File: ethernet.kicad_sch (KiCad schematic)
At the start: 32 parts

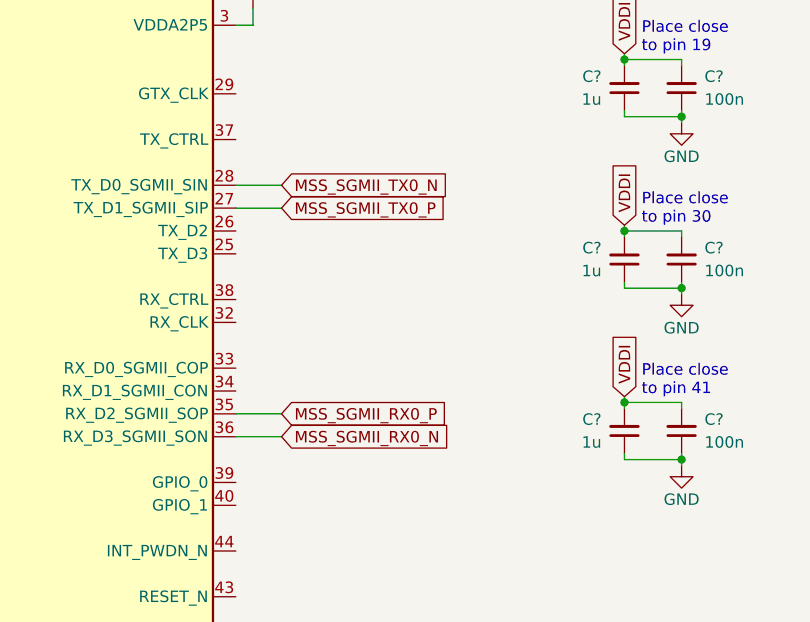
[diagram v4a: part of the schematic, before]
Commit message: [#54016] Add capacitors on SGMII lines
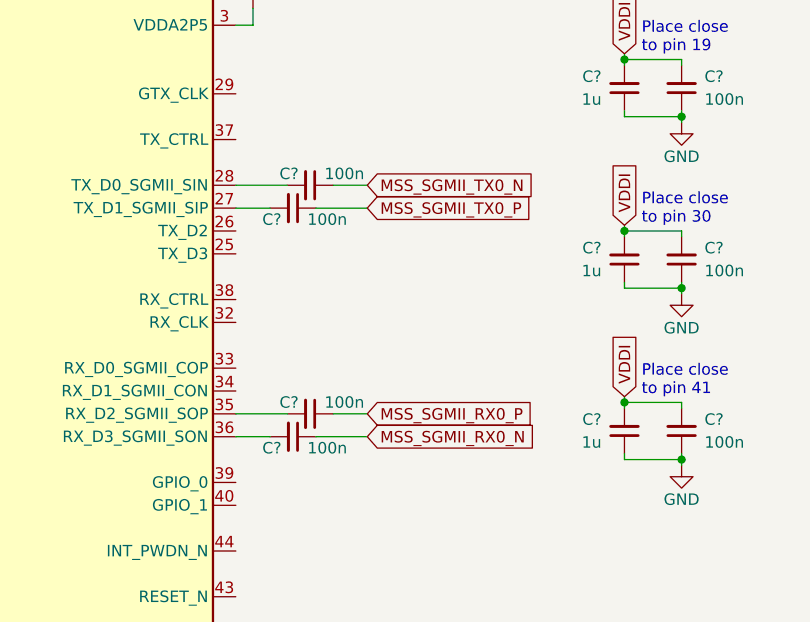
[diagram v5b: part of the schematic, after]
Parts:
- added C? (x4): C_100n_0402, antmicro-footprints:C_0402_1005Metric, symbol antmicroCapacitors0402:C_100n_0402
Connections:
- net MSS_SGMII_RX0_N: now also C?.1; no longer U?.36 (RX_D3_SGMII_SON)
- net MSS_SGMII_RX0_P: now also C?.1; no longer U?.35 (RX_D2_SGMII_SOP)
- net MSS_SGMII_TX0_N: now also C?.1; no longer U?.28 (TX_D0_SGMII_SIN)
- net MSS_SGMII_TX0_P: now also C?.1; no longer U?.27 (TX_D1_SGMII_SIP)
- new net: C?.2, U?.35 (RX_D2_SGMII_SOP)
- new net: C?.2, U?.27 (TX_D1_SGMII_SIP)
- new net: C?.2, U?.28 (TX_D0_SGMII_SIN)
- new net: C?.2, U?.36 (RX_D3_SGMII_SON)

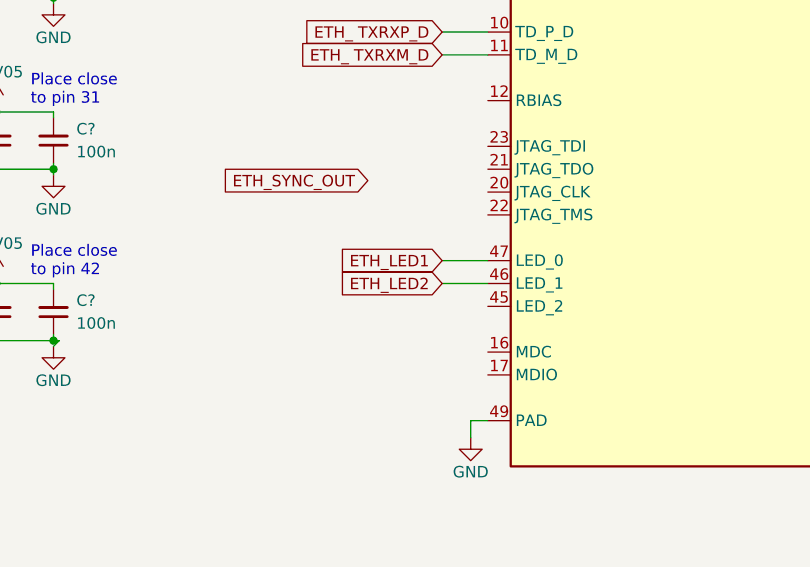
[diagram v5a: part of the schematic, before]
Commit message: [#53979] Resolve ethernet pin mapping
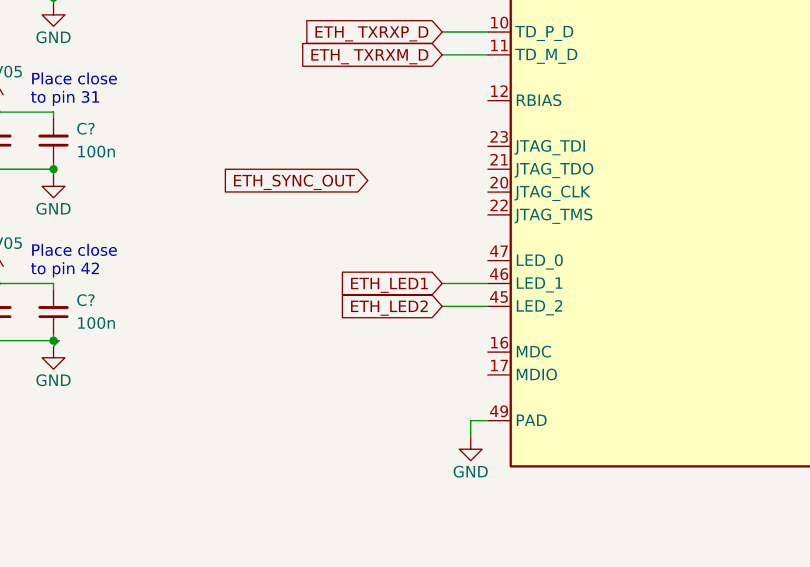
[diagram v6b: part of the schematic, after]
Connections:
- net ETH_LED1: now also U?.46 (LED_1); no longer U?.47 (LED_0)
- net ETH_LED2: now also U?.45 (LED_2); no longer U?.46 (LED_1)
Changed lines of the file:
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@@
+    (stroke (width 0) (type default) (color 0 0 0 0))
+  )
+  (wire (pts (xy 181.61 142.24) (xy 176.53 142.24))
     (stroke (width 0) (type default) (color 0 0 0 0))
   )
@@
     (stroke (width 0) (type default) (color 0 0 0 0))
   )
+  (wire (pts (xy 101.6 69.85) (xy 107.95 69.85))
+    (stroke (width 0) (type default) (color 0 0 0 0))
+  )
+  (wire (pts (xy 292.1 83.185) (xy 292.1 82.55))
+    (stroke (width 0) (type default) (color 0 0 0 0))
+  )
+  (wire (pts (xy 311.15 88.265) (xy 311.15 88.9))
+    (stroke (width 0) (type default) (color 0 0 0 0))
+  )
+  (wire (pts (xy 311.15 101.6) (xy 311.15 102.235))
+    (stroke (width 0) (type default) (color 0 0 0 0))
+  )
+  (wire (pts (xy 181.61 99.06) (xy 176.53 99.06))
+    (stroke (width 0) (type default) (color 0 0 0 0))
+  )
+  (wire (pts (xy 317.5 107.315) (xy 317.5 107.95))
+    (stroke (width 0) (type default) (color 0 0 0 0))
+  )
+  (wire (pts (xy 242.57 124.46) (xy 246.38 124.46))
+    (stroke (width 0) (type default) (color 0 0 0 0))
+  )
+  (wire (pts (xy 101.6 100.965) (xy 101.6 101.6))
+    (stroke (width 0) (type default) (color 0 0 0 0))
+  )
+  (wire (pts (xy 101.6 88.265) (xy 101.6 88.9))
+    (stroke (width 0) (type default) (color 0 0 0 0))
+  )
+  (wire (pts (xy 242.57 121.92) (xy 248.285 121.92))
+    (stroke (width 0) (type default) (color 0 0 0 0))
+  )
+  (wire (pts (xy 311.15 69.215) (xy 311.15 69.85))
+    (stroke (width 0) (type default) (color 0 0 0 0))
+  )
+  (wire (pts (xy 292.1 107.95) (xy 292.1 108.585))
+    (stroke (width 0) (type default) (color 0 0 0 0))
+  )
+  (wire (pts (xy 311.15 107.95) (xy 317.5 107.95))
+    (stroke (width 0) (type default) (color 0 0 0 0))
+  )
+  (wire (pts (xy 285.75 69.85) (xy 292.1 69.85))
+    (stroke (width 0) (type default) (color 0 0 0 0))
+  )
+  (wire (pts (xy 127 101.6) (xy 127 102.235))
+    (stroke (width 0) (type default) (color 0 0 0 0))
+  )
+  (wire (pts (xy 107.95 88.265) (xy 107.95 88.9))
+    (stroke (width 0) (type default) (color 0 0 0 0))
+  )
+  (wire (pts (xy 285.75 101.6) (xy 292.1 101.6))
+    (stroke (width 0) (type default) (color 0 0 0 0))
+  )
   (wire (pts (xy 181.61 139.7) (xy 176.53 139.7))
-    (stroke (width 0) (type default) (color 0 0 0 0))
-  )
-  (wire (pts (xy 101.6 69.85) (xy 107.95 69.85))
-    (stroke (width 0) (type default) (color 0 0 0 0))
-  )
-  (wire (pts (xy 292.1 83.185) (xy 292.1 82.55))
-    (stroke (width 0) (type default) (color 0 0 0 0))
-  )
-  (wire (pts (xy 311.15 88.265) (xy 311.15 88.9))
-    (stroke (width 0) (type default) (color 0 0 0 0))
-  )
-  (wire (pts (xy 311.15 101.6) (xy 311.15 102.235))
-    (stroke (width 0) (type default) (color 0 0 0 0))
-  )
-  (wire (pts (xy 181.61 99.06) (xy 176.53 99.06))
-    (stroke (width 0) (type default) (color 0 0 0 0))
-  )
-  (wire (pts (xy 317.5 107.315) (xy 317.5 107.95))
-    (stroke (width 0) (type default) (color 0 0 0 0))
-  )
-  (wire (pts (xy 181.61 137.16) (xy 176.53 137.16))
-    (stroke (width 0) (type default) (color 0 0 0 0))
-  )
-  (wire (pts (xy 242.57 124.46) (xy 246.38 124.46))
-    (stroke (width 0) (type default) (color 0 0 0 0))
-  )
-  (wire (pts (xy 101.6 100.965) (xy 101.6 101.6))
-    (stroke (width 0) (type default) (color 0 0 0 0))
-  )
-  (wire (pts (xy 101.6 88.265) (xy 101.6 88.9))
-    (stroke (width 0) (type default) (color 0 0 0 0))
-  )
-  (wire (pts (xy 242.57 121.92) (xy 248.285 121.92))
-    (stroke (width 0) (type default) (color 0 0 0 0))
-  )
-  (wire (pts (xy 311.15 69.215) (xy 311.15 69.85))
-    (stroke (width 0) (type default) (color 0 0 0 0))
-  )
-  (wire (pts (xy 292.1 107.95) (xy 292.1 108.585))
-    (stroke (width 0) (type default) (color 0 0 0 0))
-  )
-  (wire (pts (xy 311.15 107.95) (xy 317.5 107.95))
-    (stroke (width 0) (type default) (color 0 0 0 0))
-  )
-  (wire (pts (xy 285.75 69.85) (xy 292.1 69.85))
-    (stroke (width 0) (type default) (color 0 0 0 0))
-  )
-  (wire (pts (xy 127 101.6) (xy 127 102.235))
-    (stroke (width 0) (type default) (color 0 0 0 0))
-  )
-  (wire (pts (xy 107.95 88.265) (xy 107.95 88.9))
-    (stroke (width 0) (type default) (color 0 0 0 0))
-  )
-  (wire (pts (xy 285.75 101.6) (xy 292.1 101.6))
     (stroke (width 0) (type default) (color 0 0 0 0))
   )
@@
     )
   )
-  (global_label "ETH_LED2" (shape input) (at 176.53 139.7 180) (fields_autoplaced)
-    (effects (font (size 1.27 1.27)) (justify right))
-    (property "Intersheet References" "${INTERSHEET_REFS}" (id 0) (at 165.0455 139.6206 0)
-      (effects (font (size 1.27 1.27)) (justify right) hide)
-    )
-  )
   (global_label "ETH_TXRXM_B" (shape input) (at 176.53 99.06 180) (fields_autoplaced)
     (effects (font (size 1.27 1.27)) (justify right))
@@
     )
   )
+  (global_label "ETH_LED2" (shape input) (at 176.53 142.24 180) (fields_autoplaced)
+    (effects (font (size 1.27 1.27)) (justify right))
+    (property "Intersheet References" "${INTERSHEET_REFS}" (id 0) (at 165.0455 142.1606 0)
+      (effects (font (size 1.27 1.27)) (justify right) hide)
+    )
+  )
   (global_label "ETH_TXRXP_A" (shape input) (at 176.53 88.9 180) (fields_autoplaced)
     (effects (font (size 1.27 1.27)) (justify right))
@@
     )
   )
+  (global_label "ETH_LED1" (shape input) (at 176.53 139.7 180) (fields_autoplaced)
+    (effects (font (size 1.27 1.27)) (justify right))
+    (property "Intersheet References" "${INTERSHEET_REFS}" (id 0) (at 165.0455 139.6206 0)
+      (effects (font (size 1.27 1.27)) (justify right) hide)
+    )
+  )
   (global_label "MSS_SGMII_TX0_P" (shape input) (at 239.395 222.25 0) (fields_autoplaced)
     (effects (font (size 1.27 1.27)) (justify left))
@@
     )
   )
-  (global_label "ETH_LED1" (shape input) (at 176.53 137.16 180) (fields_autoplaced)
-    (effects (font (size 1.27 1.27)) (justify right))
-    (property "Intersheet References" "${INTERSHEET_REFS}" (id 0) (at 165.0455 137.0806 0)
-      (effects (font (size 1.27 1.27)) (justify right) hide)
-    )
-  )
